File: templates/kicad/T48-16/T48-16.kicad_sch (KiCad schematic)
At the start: 16 parts

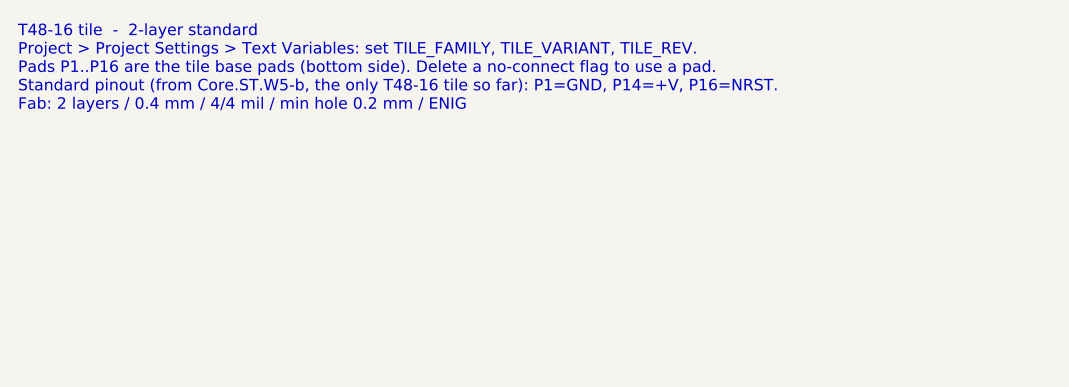
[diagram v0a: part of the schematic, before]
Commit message: Re-tier on measured prices: 4L on 0.2 mm drill, add 4L-fine
4L keeps the 0.2 mm drill so it lands in PCBWay's $162 standard bucket
rather than the $419 one; 3/3 mil and 0.15 mm drills move to a new 4L-fine
tier on the advanced form. Quotes name the calculator to use. set_tier.py
gains --package for projects that predate the templates and --ignore-locks
for stale lock files.

Co-Authored-By: Claude Fable 5.1 <noreply@anthropic.com>
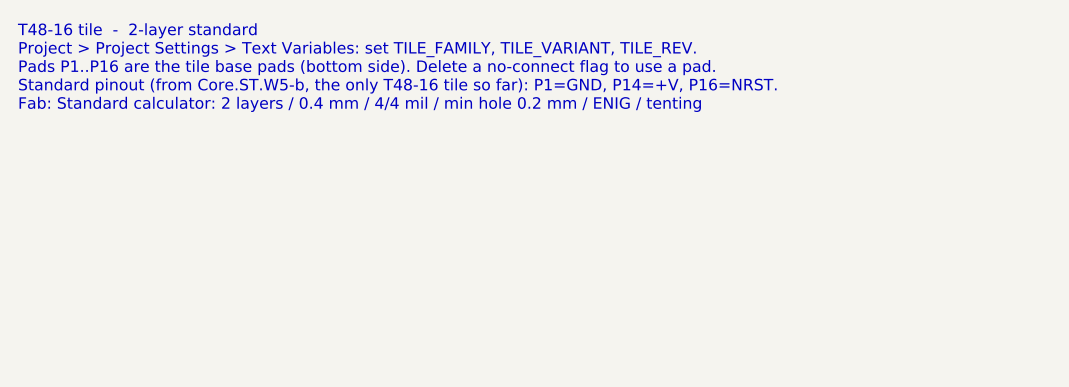
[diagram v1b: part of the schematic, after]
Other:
- note added: "T48-16 tile - 2-layer standard Project > Project Settings > Text Variables: set TILE_FAMILY, TILE_VARIANT, TILE_REV. Pads P1..P16 are the tile base pads (bottom side). Delete a no-connect flag to use a pad. Standard pinout (from Core.ST.W5-b, the only T48-16 tile so far): P1=GND, P14=+V, P16=NRST. Fab: Standard calculator: 2 layers / 0.4 mm / 4/4 mil / min hole 0.2 mm / ENIG / tenting"
- note removed: "T48-16 tile - 2-layer standard Project > Project Settings > Text Variables: set TILE_FAMILY, TILE_VARIANT, TILE_REV. Pads P1..P16 are the tile base pads (bottom side). Delete a no-connect flag to use a pad. Standard pinout (from Core.ST.W5-b, the only T48-16 tile so far): P1=GND, P14=+V, P16=NRST. Fab: 2 layers / 0.4 mm / 4/4 mil / min hole 0.2 mm / ENIG"
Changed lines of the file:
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@@
 		(comment 2 "${FAB_QUOTE}")
 	)
-	(text "T48-16 tile  -  2-layer standard\nProject > Project Settings > Text Variables: set TILE_FAMILY, TILE_VARIANT, TILE_REV.\nPads P1..P16 are the tile base pads (bottom side). Delete a no-connect flag to use a pad.\nStandard pinout (from Core.ST.W5-b, the only T48-16 tile so far): P1=GND, P14=+V, P16=NRST.\nFab: 2 layers / 0.4 mm / 4/4 mil / min hole 0.2 mm / ENIG"
+	(text "T48-16 tile  -  2-layer standard\nProject > Project Settings > Text Variables: set TILE_FAMILY, TILE_VARIANT, TILE_REV.\nPads P1..P16 are the tile base pads (bottom side). Delete a no-connect flag to use a pad.\nStandard pinout (from Core.ST.W5-b, the only T48-16 tile so far): P1=GND, P14=+V, P16=NRST.\nFab: Standard calculator: 2 layers / 0.4 mm / 4/4 mil / min hole 0.2 mm / ENIG / tenting"
 		(exclude_from_sim no)
 		(at 25.4 25.4 0)
